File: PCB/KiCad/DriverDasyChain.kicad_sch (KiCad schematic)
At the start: 52 parts, among them J1 Conn_01x03, J10 Conn_01x04, J12 Conn_01x04, J2 Conn_01x03, J3 Conn_01x03, J4 Conn_01x04, J5 Conn_01x03, J6 Conn_01x04, Q2 IRLR3410TRPBF, SW1 SW_DIP_x02, SW2 SW_SPDT, U1 AP2112K-3.3, U2 XIAO-ESP32-S3-DIP, U3 74AHCT1G125, U4 SN65HVD230

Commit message: Update PCB daisy chain documentation and layout details
- Enhanced power distribution details for the daisy chain, including updated capacitor specifications for bulk capacitance.
- Clarified the layout topology for the braking circuit and updated the placement of the flyback diode.
- Added a CAN-TVS protection component to the schematic and layout, ensuring proper placement for transceiver protection.
- Verified and documented layout standards, including ground and power plane considerations, and ensured compliance with IPC-2221 standards.
- Updated the status of various tasks related to the PCB design, including completion of split-termination and CAN-TVS integration.
- Added a lock file for the KiCad PCB project to track user access.
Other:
- note added: "M2 Löcher zum fest- schrauben an den Treiber"
- note added: "Mounting Hole"
- note removed: "Mouting Holes"
- moved on the sheet: C1, C10, C13, C14, C2, C3, C5, C6, C8, D2, D3, H1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

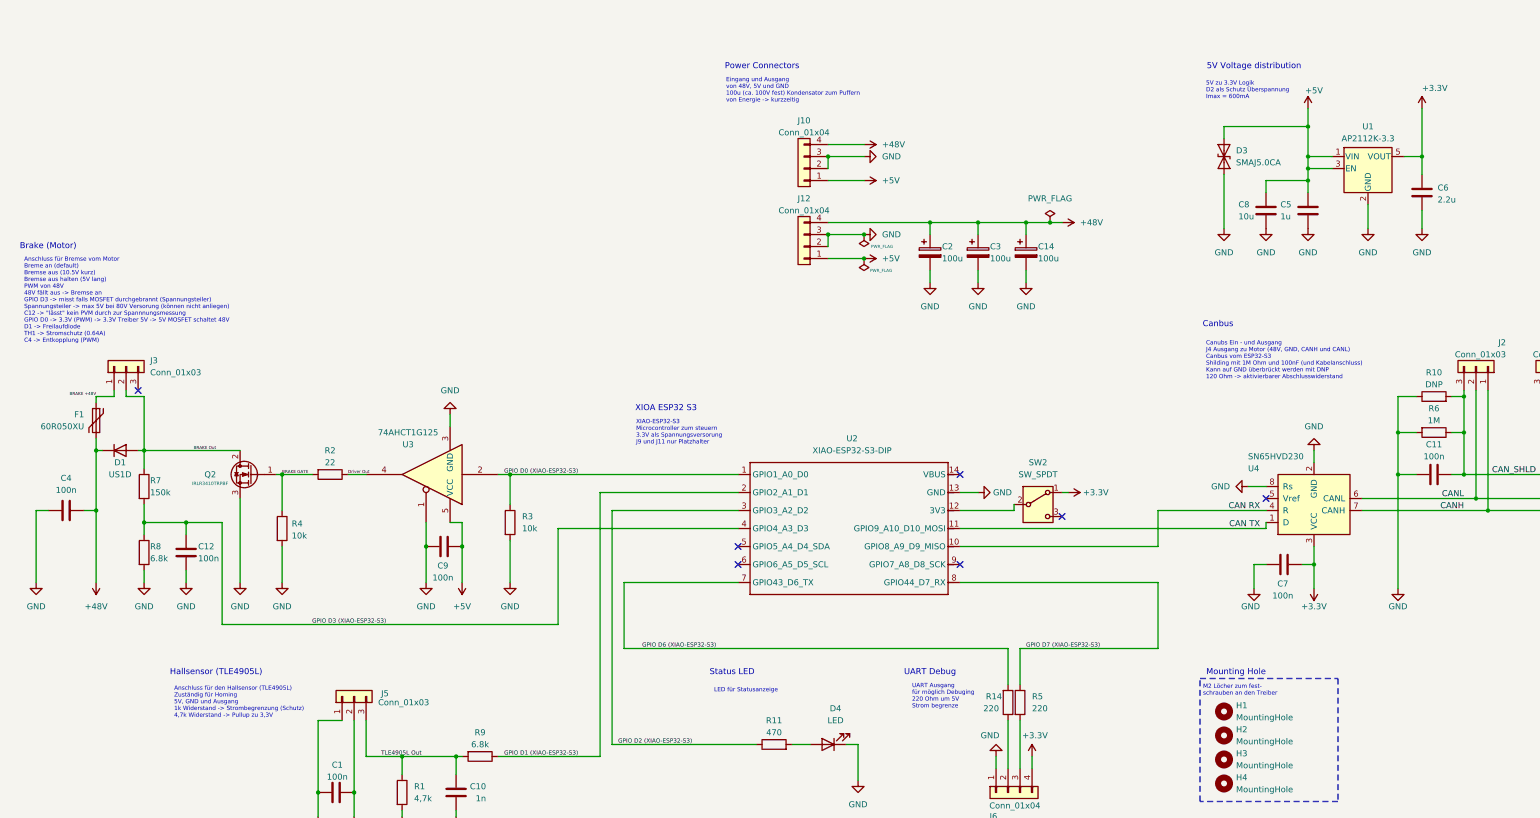
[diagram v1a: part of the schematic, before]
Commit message: Update PCB documentation and design for improved safety and performance
- Clarified CAN pin assignments and wiring for GDS68 and RS05 drivers.
- Added notes on the benign nature of terminal swapping at J4, J10, and J12.
- Revised D1 placement explanation to emphasize its role and impact on braking performance.
- Enhanced safety notes regarding the 48 V power supply and potential risks of incorrect wiring.
- Specified the use of Nexperia PESD12VL2BT for CAN bus protection, detailing its specifications and placement.
- Updated capacitor recommendations for 48 V buffer capacitors, emphasizing the importance of ripple current ratings and temperature resilience.
- Adjusted BOM entries for capacitors to reflect alternative options and quantities needed.
- Documented changes to PCB layout and design rules, ensuring compliance with safety standards.
- Addressed open points regarding the schematic and layout, including ERC warnings and component placements.
- Emphasized the need for thorough testing and verification before powering up the system.
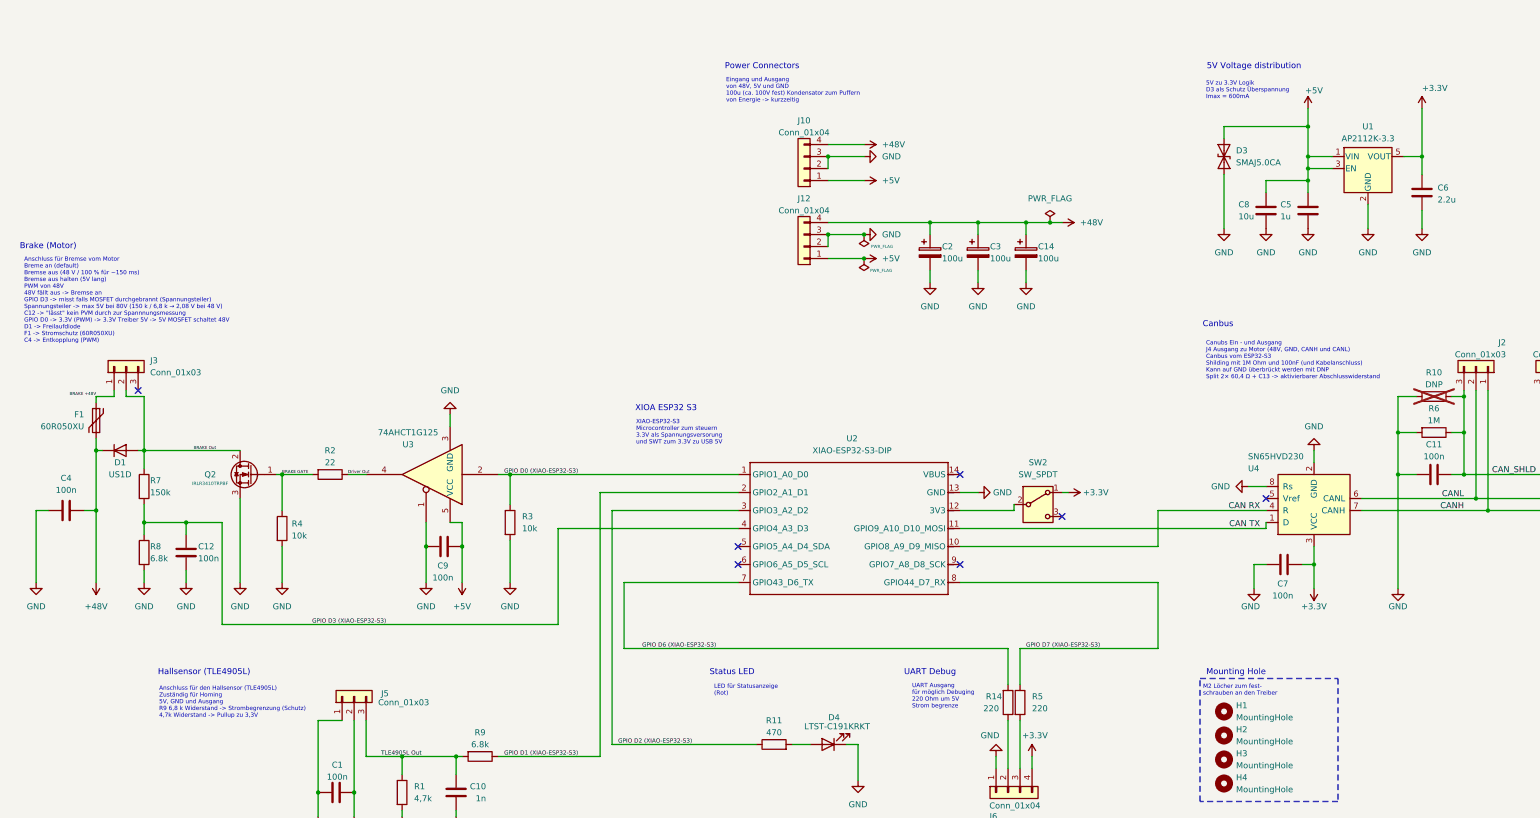
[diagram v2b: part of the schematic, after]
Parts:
- C4: Note (none) -> mind. 100V Spannungsfest
- D4: value LED -> LTST-C191KRKT
- J4: Note (none) -> Leiterquerschnitt Motorabzweig, 1,5 mm² Power + 0,5 mm² CAN
- R10: now not fitted
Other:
- note added: "5V zu 3.3V Logik D3 als Schutz Überspannung Imax = 600mA"
- note added: "Anschluss für Bremse vom Motor Breme an (default) Bremse aus (48 V / 100 % für ~150 ms) Bremse aus halten (5V lang) PWM von 48V 48V fällt aus -> Bremse an GPIO D3 -> misst falls MOSFET durchgebrannt (Spannungsteiler) Spannungsteiler -> max 5V bei 80V (150 k / 6,8 k → 2,08 V bei 48 V) C12 -> "lässt" kein PVM durch zur Spannnungsmessung GPIO D0 -> 3.3V (PWM) -> 3.3V Treiber 5V -> 5V MOSFET schaltet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"
- note added: "Anschluss für den Hallsensor (TLE4905L) Zuständig für Homing 5V, GND und Ausgang R9 6,8 k Widerstand -> Strombegrenzung (Schutz) 4,7k Widerstand -> Pullup zu 3,3V"
- note added: "Canubs Ein - und Ausgang J4 Ausgang zu Motor (48V, GND, CANH und CANL) Canbus vom ESP32-S3 Shilding mit 1M Ohm und 100nF (und Kabelanschluss) Kann auf GND überbrückt werden mit DNP Split 2× 60,4 Ω + C13 -> aktivierbarer Abschlusswiderstand"
- note added: "LED für Statusanzeige (Rot)"
- note added: "XIAO-ESP32-S3 Microcontroller zum steuern 3.3V als Spannungsversorung und SWT zum 3.3V zu USB 5V"
- note removed: "5V zu 3.3V Logik D2 als Schutz Überspannung Imax = 600mA"
- note removed: "Anschluss für Bremse vom Motor Breme an (default) Bremse aus (10.5V kurz) Bremse aus halten (5V lang) PWM von 48V 48V fällt aus -> Bremse an GPIO D3 -> misst falls MOSFET durchgebrannt (Spannungsteiler) Spannungsteiler -> max 5V bei 80V Versorung (können nicht anliegen) C12 -> "lässt" kein PVM durch zur Spannnungsmessung GPIO D0 -> 3.3V (PWM) -> 3.3V Treiber 5V -> 5V MOSFET schaltet 48V D1 -> Fre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"
- note removed: "Anschluss für den Hallsensor (TLE4905L) Zuständig für Homing 5V, GND und Ausgang 1k Widerstand -> Strombegrenzung (Schutz) 4,7k Widerstand -> Pullup zu 3,3V"
- note removed: "Canubs Ein - und Ausgang J4 Ausgang zu Motor (48V, GND, CANH und CANL) Canbus vom ESP32-S3 Shilding mit 1M Ohm und 100nF (und Kabelanschluss) Kann auf GND überbrückt werden mit DNP 120 Ohm -> aktivierbarer Abschlusswiderstand"
- note removed: "LED für Statusanzeige"
- note removed: "XIAO-ESP32-S3 Microcontroller zum steuern 3.3V als Spannungsversorung J9 und J11 nur Platzhalter"
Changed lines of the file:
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@@
 		)
 	)
-	(text "XIAO-ESP32-S3\nMicrocontroller zum steuern\n3.3V als Spannungsversorung \nJ9 und J11 nur Platzhalter"
+	(text "XIAO-ESP32-S3\nMicrocontroller zum steuern\n3.3V als Spannungsversorung \nund SWT zum 3.3V zu USB 5V"
 		(exclude_from_sim no)
 		(at 151.13 148.59 0)
@@
 	(text "Hallsensor (TLE4905L)"
 		(exclude_from_sim no)
-		(at 62.23 199.39 0)
+		(at 59.69 199.39 0)
 		(effects
 			(font
@@
 		)
 	)
-	(text "Anschluss für Bremse vom Motor\nBreme an (default)\nBremse aus (10.5V kurz)\nBremse aus halten (5V lang)\nPWM von 48V \n48V fällt aus -> Bremse an\nGPIO D3 -> misst falls MOSFET durchgebrannt (Spannungsteiler)\nSpannungsteiler -> max 5V bei 80V Versorung (können nicht anliegen)\nC12 -> \"lässt\" kein PVM durch zur Spannnungsmessung\nGPIO D0 -> 3.3V (PWM) -> 3.3V Treiber 5V -> 5V MOSFET schaltet 48V\nD1 -> Freilaufdiode\nTH1 -> Stromschutz (0.64A)\nC4 -> Entkopplung (PWM)"
+	(text "Anschluss für Bremse vom Motor\nBreme an (default)\nBremse aus (48 V / 100 % für ~150 ms)\nBremse aus halten (5V lang)\nPWM von 48V \n48V fällt aus -> Bremse an\nGPIO D3 -> misst falls MOSFET durchgebrannt (Spannungsteiler)\nSpannungsteiler -> max 5V bei 80V (150 k / 6,8 k → 2,08 V bei 48 V)\nC12 -> \"lässt\" kein PVM durch zur Spannnungsmessung\nGPIO D0 -> 3.3V (PWM) -> 3.3V Treiber 5V -> 5V MOSFET schaltet 48V\nD1 -> Freilaufdiode\nF1 -> Stromschutz (60R050XU)\nC4 -> Entkopplung (PWM)"
 		(exclude_from_sim no)
 		(at 21.59 120.65 0)
@@
 		)
 	)
-	(text "Canubs Ein - und Ausgang\nJ4 Ausgang zu Motor (48V, GND, CANH und CANL)\nCanbus vom ESP32-S3\nShilding mit 1M Ohm und 100nF (und Kabelanschluss)\nKann auf GND überbrückt werden mit DNP\n120 Ohm -> aktivierbarer Abschlusswiderstand\n"
+	(text "Canubs Ein - und Ausgang\nJ4 Ausgang zu Motor (48V, GND, CANH und CANL)\nCanbus vom ESP32-S3\nShilding mit 1M Ohm und 100nF (und Kabelanschluss)\nKann auf GND überbrückt werden mit DNP\nSplit 2× 60,4 Ω + C13 -> aktivierbarer Abschlusswiderstand\n"
 		(exclude_from_sim no)
 		(at 271.78 133.35 0)
@@
 		)
 	)
-	(text "5V zu 3.3V Logik\nD2 als Schutz Überspannung\nImax = 600mA"
+	(text "5V zu 3.3V Logik\nD3 als Schutz Überspannung\nImax = 600mA"
 		(exclude_from_sim no)
 		(at 271.78 76.2 0)
@@
 		)
 	)
-	(text "LED für Statusanzeige"
+	(text "LED für Statusanzeige\n(Rot)"
 		(exclude_from_sim no)
 		(at 167.64 203.2 0)
@@
 		)
 	)
-	(text "Anschluss für den Hallsensor (TLE4905L)\nZuständig für Homing\n5V, GND und Ausgang \n1k Widerstand -> Strombegrenzung (Schutz)\n4,7k Widerstand -> Pullup zu 3,3V"
+	(text "Anschluss für den Hallsensor (TLE4905L)\nZuständig für Homing\n5V, GND und Ausgang \nR9 6,8 k Widerstand -> Strombegrenzung (Schutz)\n4,7k Widerstand -> Pullup zu 3,3V"
 		(exclude_from_sim no)
-		(at 53.34 205.74 0)
+		(at 50.165 205.74 0)
 		(effects
 			(font
@@
 		(polyline
 			(pts
-				(xy 142.24 200.66) (xy 52.07 200.66) (xy 52.07 240.03) (xy 142.24 240.03)
+				(xy 142.24 200.66) (xy 48.895 200.66) (xy 48.895 240.03) (xy 142.24 240.03)
 			)
 			(stroke
@@
 			)
 		)
+		(property "Note" "mind. 100V Spannungsfest"
+			(at 30.48 165.1 90)
+			(hide yes)
+			(show_name no)
+			(do_not_autoplace no)
+			(effects
+				(font
+					(size 1.27 1.27)
+				)
+			)
+		)
 		(pin "2"
 		)
@@
 		(in_pos_files yes)
 		(dnp no)
-		(fields_autoplaced yes)
 		(property "Reference" "D4"
-			(at 193.3575 207.01 0)
+			(at 193.04 208.915 0)
 			(show_name no)
 			(do_not_autoplace no)
@@
 			)
 		)
-		(property "Value" "LED"
-			(at 193.3575 209.55 0)
+		(property "Value" "LTST-C191KRKT"
+			(at 193.675 210.82 0)
 			(show_name no)
 			(do_not_autoplace no)
@@
 			)
 		)
+		(property "Note" "Leiterquerschnitt Motorabzweig, 1,5 mm² Power + 0,5 mm² CAN"
+			(at 363.22 134.62 90)
+			(hide yes)
+			(show_name no)
+			(do_not_autoplace no)
+			(effects
+				(font
+					(size 1.27 1.27)
+				)
+			)
+		)
 		(pin "4"
 		)
@@
 		(on_board yes)
 		(in_pos_files yes)
-		(dnp no)
+		(dnp yes)
 		(property "Reference" "R10"
 			(at 320.04 135.89 90)
